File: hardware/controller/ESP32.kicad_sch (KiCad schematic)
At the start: 22 parts, among them J4 Conn_01x05_Pin, Q1 SS8050-G, Q2 SS8050-G, U2 ESP32-S3, Y1 FH4000074Z

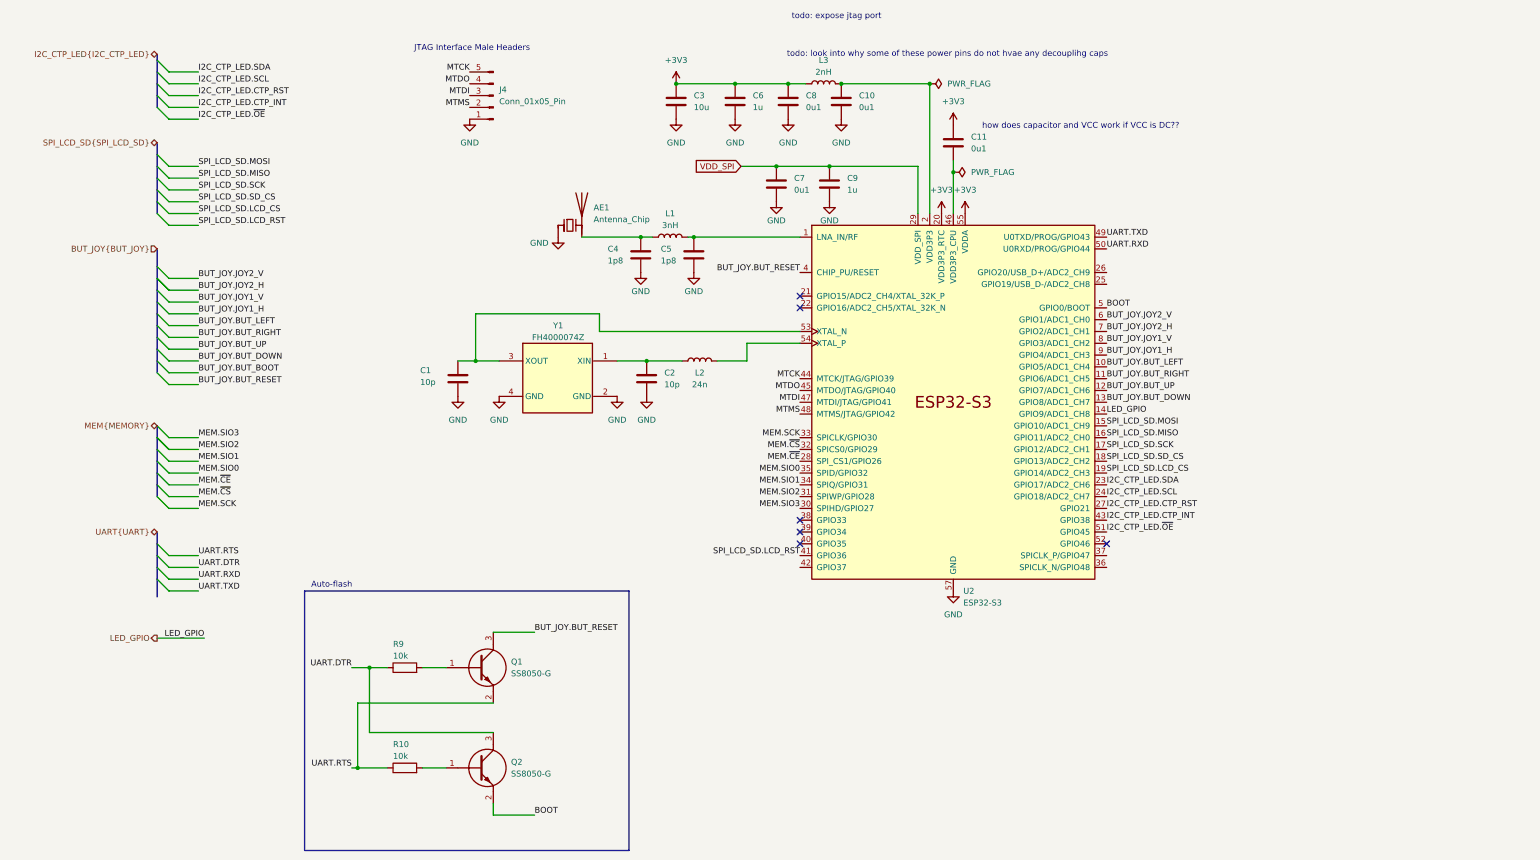
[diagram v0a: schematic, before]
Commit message: finished first rev of controller schematic minus actually finding passive components. moved some features to rev2 todo
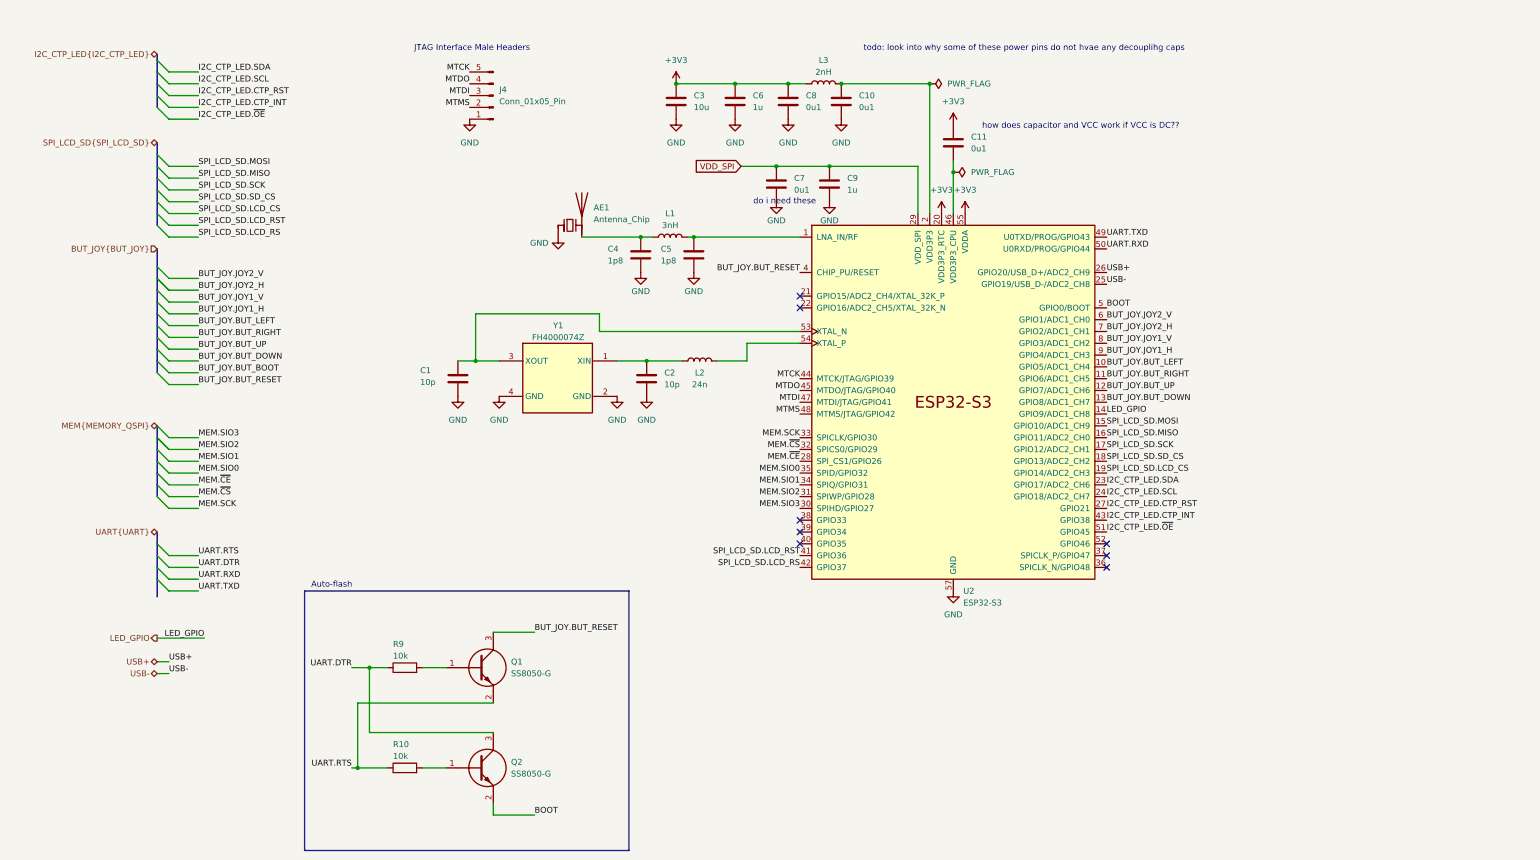
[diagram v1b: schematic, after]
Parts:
- AE1: footprint RF_Antenna:Texas_SWRA117D_2.4GHz_Right -> RF_Antenna:Texas_SWRA117D_2.4GHz_Left
- U2: footprint Package_DFN_QFN:QFN-56-1EP_7x7mm_P0.4mm_EP5.6x5.6mm -> SamacSys_Parts:QFN-56-1EP_7x7mm_P0.4mm_EP5.6x5.6mm
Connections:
- net USB-: now reaches U2.25 (GPIO19/USB_D-/ADC2_CH8)
- net USB+: now reaches U2.26 (GPIO20/USB_D+/ADC2_CH9)
- net SPI_LCD_SD.LCD_RS: now reaches U2.42 (GPIO37)
- no-connect marks 6 -> 8
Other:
- note added: "do i need these"
- note removed: "todo: expose jtag port"
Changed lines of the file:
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@@
 	(generator_version "9.0")
 	(paper "A4")
-	(bus_alias "MEMORY"
+	(bus_alias "MEMORY_QSPI"
 		(members "~{CS}" "~{CE}" "SIO0" "SCK" "SIO1" "SIO2" "SIO3")
 	)
@@
 	(text "todo: look into why some of these power pins do not hvae any decouplihg caps"
 		(exclude_from_sim no)
-		(at 213.36 22.86 0)
+		(at 229.87 21.59 0)
 		(effects
 			(font
@@
 		)
 	)
-	(text "todo: expose jtag port\n"
+	(text "do i need these"
 		(exclude_from_sim no)
-		(at 189.484 14.732 0)
+		(at 178.308 54.61 0)
 		(effects
 			(font
@@
 	)
 	(no_connect
+		(at 247.65 130.81)
+	)
+	(no_connect
 		(at 247.65 128.27)
 	)
@@
 	)
 	(no_connect
+		(at 247.65 133.35)
+	)
+	(no_connect
 		(at 181.61 123.19)
 	)
@@
 	)
 	(bus_entry
+		(at 43.18 59.69)
+		(size 2.54 2.54)
+		(stroke
+			(width 0)
+			(type default)
+		)
+	)
+	(bus_entry
 		(at 43.18 130.81)
 		(size 2.54 2.54)
@@
 	(wire
 		(pts
+			(xy 45.72 156.21) (xy 43.18 156.21)
+		)
+		(stroke
+			(width 0)
+			(type default)
+		)
+	)
+	(wire
+		(pts
 			(xy 45.72 107.95) (xy 52.07 107.95)
 		)
@@
 	(wire
 		(pts
+			(xy 45.72 62.23) (xy 52.07 62.23)
+		)
+		(stroke
+			(width 0)
+			(type default)
+		)
+	)
+	(wire
+		(pts
 			(xy 45.72 93.98) (xy 52.07 93.98)
 		)
@@
 		)
 	)
+	(wire
+		(pts
+			(xy 43.18 153.67) (xy 45.72 153.67)
+		)
+		(stroke
+			(width 0)
+			(type default)
+		)
+	)
 	(bus
 		(pts
@@
 		)
 	)
-	(wire
-		(pts
-			(xy 187.96 46.99) (xy 207.01 46.99)
-		)
-		(stroke
-			(width 0)
-			(type default)
-		)
-	)
 	(bus
 		(pts
@@
 	(wire
 		(pts
+			(xy 187.96 46.99) (xy 207.01 46.99)
+		)
+		(stroke
+			(width 0)
+			(type default)
+		)
+	)
+	(wire
+		(pts
 			(xy 138.43 82.55) (xy 138.43 78.74)
 		)
@@
 		)
 	)
+	(bus
+		(pts
+			(xy 43.18 57.15) (xy 43.18 59.69)
+		)
+		(stroke
+			(width 0)
+			(type default)
+		)
+	)
 	(label "MEM.SIO2"
 		(at 181.61 118.11 180)
@@
 		)
 	)
+	(label "USB-"
+		(at 45.72 156.21 0)
+		(effects
+			(font
+				(size 1.27 1.27)
+			)
+			(justify left bottom)
+		)
+	)
 	(label "BUT_JOY.JOY1_H"
 		(at 247.65 87.63 0)
@@
 		)
 	)
+	(label "USB+"
+		(at 247.65 69.85 0)
+		(effects
+			(font
+				(size 1.27 1.27)
+			)
+			(justify left bottom)
+		)
+	)
 	(label "BUT_JOY.BUT_LEFT"
 		(at 52.07 81.28 0)
@@
 		)
 	)
+	(label "SPI_LCD_SD.LCD_RS"
+		(at 181.61 133.35 180)
+		(effects
+			(font
+				(size 1.27 1.27)
+			)
+			(justify right bottom)
+		)
+	)
 	(label "BUT_JOY.JOY1_V"
 		(at 247.65 85.09 0)
@@
 		)
 	)
+	(label "USB+"
+		(at 45.72 153.67 0)
+		(effects
+			(font
+				(size 1.27 1.27)
+			)
+			(justify left bottom)
+		)
+	)
 	(label "I2C_CTP_LED.SDA"
 		(at 247.65 115.57 0)
@@
 		)
 	)
+	(label "SPI_LCD_SD.LCD_RS"
+		(at 52.07 62.23 0)
+		(effects
+			(font
+				(size 1.27 1.27)
+			)
+			(justify left bottom)
+		)
+	)
 	(label "MEM.SCK"
 		(at 181.61 105.41 180)
@@
 		)
 	)
+	(label "USB-"
+		(at 247.65 72.39 0)
+		(effects
+			(font
+				(size 1.27 1.27)
+			)
+			(justify left bottom)
+		)
+	)
 	(label "BUT_JOY.BUT_RIGHT"
 		(at 52.07 83.82 0)
@@
 		)
 	)
-	(hierarchical_label "MEM{MEMORY}"
+	(hierarchical_label "USB+"
+		(shape bidirectional)
+		(at 43.18 153.67 180)
+		(effects
+			(font
+				(size 1.27 1.27)
+			)
+			(justify right)
+		)
+	)
+	(hierarchical_label "MEM{MEMORY_QSPI}"
 		(shape bidirectional)
 		(at 43.18 102.87 180)
@@
 		)
 	)
+	(hierarchical_label "USB-"
+		(shape bidirectional)
+		(at 43.18 156.21 180)
+		(effects
+			(font
+				(size 1.27 1.27)
+			)
+			(justify right)
+		)
+	)
 	(hierarchical_label "SPI_LCD_SD{SPI_LCD_SD}"
 		(shape bidirectional)
@@
 			)
 		)
-		(property "Footprint" "RF_Antenna:Texas_SWRA117D_2.4GHz_Right"
+		(property "Footprint" "RF_Antenna:Texas_SWRA117D_2.4GHz_Left"
 			(at 129.54 55.245 0)
 			(effects
@@
 			)
 		)
-		(property "Footprint" "Package_DFN_QFN:QFN-56-1EP_7x7mm_P0.4mm_EP5.6x5.6mm"
+		(property "Footprint" "SamacSys_Parts:QFN-56-1EP_7x7mm_P0.4mm_EP5.6x5.6mm"
 			(at 214.63 146.05 0)
 			(effects

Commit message: Moved LEDs around. Replaced some discrete resistors with resistor arrays. Added mounting holes. Added. Added a lot of actual components for passive elements
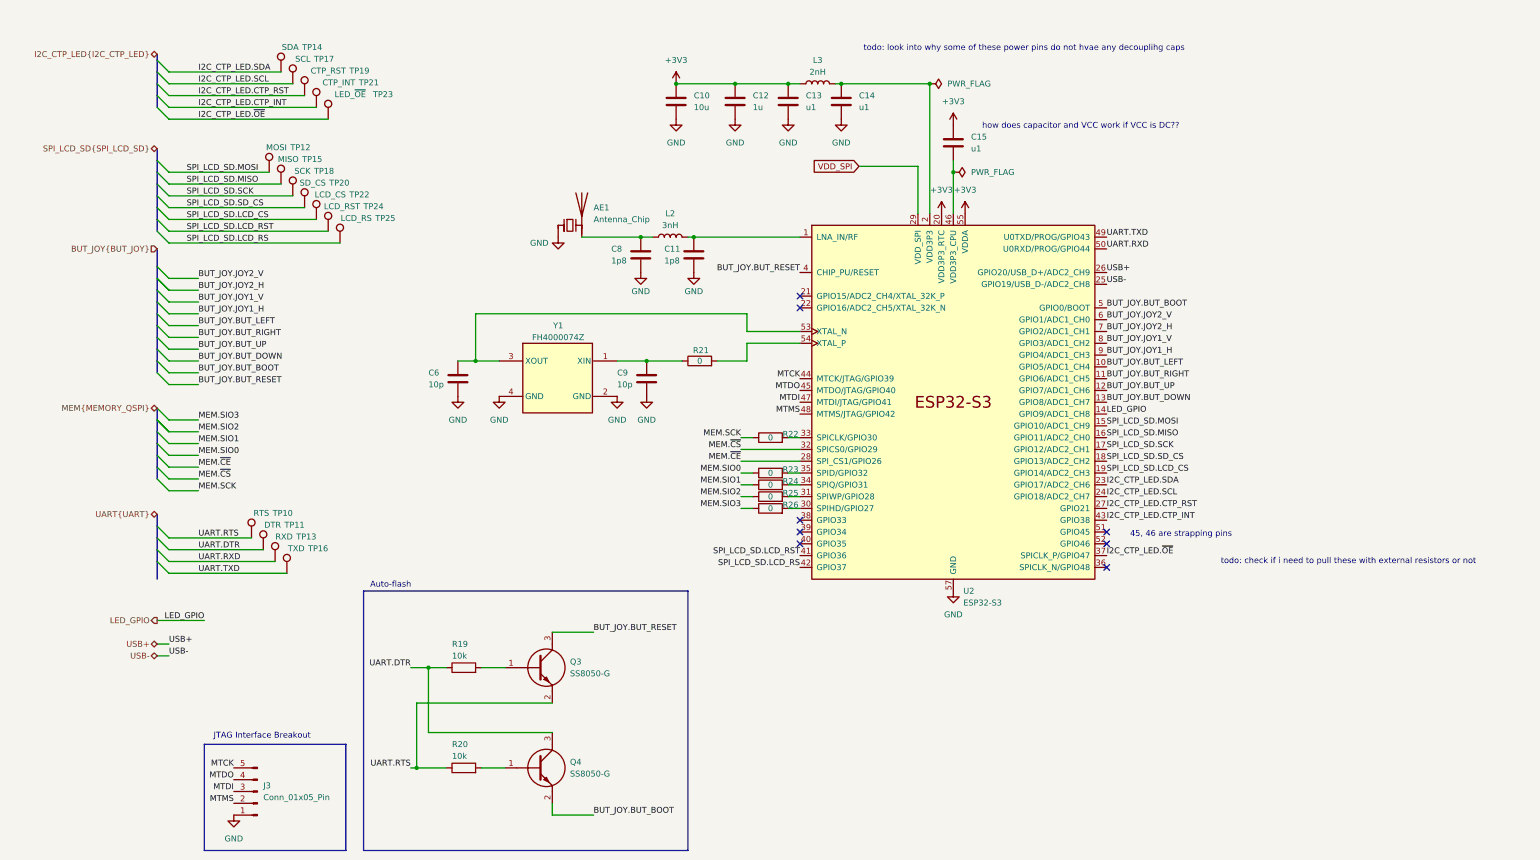
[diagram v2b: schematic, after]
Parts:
- removed C1, C2: 10p, symbol Device:C
- removed C4, C5: 1p8, symbol Device:C
- removed C7: 0u1, symbol Device:C
- removed L2: 24n, symbol Device:L
- added C11, C8: 1p8, Capacitor_SMD:C_0603_1608Metric, symbol Device:C
- added C6: 10p, GRT033, symbol Device:C
- added R21, R22, R23, R24, R25, R26: 0, RESC1608X50N, symbol Device:R
- added TP10: RTS, TestPoint:TestPoint_Pad_1.0x1.0mm, symbol Connector:TestPoint
- added TP11: DTR, TestPoint:TestPoint_Pad_1.0x1.0mm, symbol Connector:TestPoint
- added TP12: MOSI, TestPoint:TestPoint_Pad_1.0x1.0mm, symbol Connector:TestPoint
- added TP13: RXD, TestPoint:TestPoint_Pad_1.0x1.0mm, symbol Connector:TestPoint
- added TP14: SDA, TestPoint:TestPoint_Pad_1.0x1.0mm, symbol Connector:TestPoint
- added TP15: MISO, TestPoint:TestPoint_Pad_1.0x1.0mm, symbol Connector:TestPoint
- added TP16: TXD, TestPoint:TestPoint_Pad_1.0x1.0mm, symbol Connector:TestPoint
- added TP17: SCL, TestPoint:TestPoint_Pad_1.0x1.0mm, symbol Connector:TestPoint
- added TP18: SCK, TestPoint:TestPoint_Pad_1.0x1.0mm, symbol Connector:TestPoint
- added TP19: CTP_RST, TestPoint:TestPoint_Pad_1.0x1.0mm, symbol Connector:TestPoint
- added TP20: SD_CS, TestPoint:TestPoint_Pad_1.0x1.0mm, symbol Connector:TestPoint
- added TP21: CTP_INT, TestPoint:TestPoint_Pad_1.0x1.0mm, symbol Connector:TestPoint
- added TP22: LCD_CS, TestPoint:TestPoint_Pad_1.0x1.0mm, symbol Connector:TestPoint
- added TP23: LED_~{OE}, TestPoint:TestPoint_Pad_1.0x1.0mm, symbol Connector:TestPoint
- added TP24: LCD_RST, TestPoint:TestPoint_Pad_1.0x1.0mm, symbol Connector:TestPoint
- added TP25: LCD_RS, TestPoint:TestPoint_Pad_1.0x1.0mm, symbol Connector:TestPoint
- C10: renamed from C3; footprint (none) -> CAPC1608X80N; Height (none) -> 0.8; Manufacturer_Name (none) -> TDK; Manufacturer_Part_Number (none) -> C1608X7T1A106M080AC; Mouser Part Number (none) -> 810-C1608X7T1A106M08; Mouser Price/Stock (none) -> https://www.mouser.co.uk/ProductDetail/TDK/C1608X7T1A106M08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
- C12: renamed from C6; footprint (none) -> CAPC2012X135N; Height (none) -> 1.35; Manufacturer_Name (none) -> Walsin Technology Corporation; Manufacturer_Part_Number (none) -> 0805X105K160CT; Mouser Part Number (none) -> 791-0805X105K160CT; Mouser Price/Stock (none) -> https://www.mouser.co.uk/ProductDetail/Walsin/0805X105K160C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
- C13: renamed from C8; value 0u1 -> u1; footprint (none) -> MAJx16; Height (none) -> 0.8; Manufacturer_Name (none) -> TAIYO YUDEN; Manufacturer_Part_Number (none) -> MAJCH168BB7104KTEA01; Mouser Part Number (none) -> 963-MAJCH168BB7104KT; Mouser Price/Stock (none) -> https://www.mouser.co.uk/ProductDetail/TAIYO-YUDEN/MAJCH168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
- C14: renamed from C10; value 0u1 -> u1; footprint (none) -> MAJx16; Height (none) -> 0.8; Manufacturer_Name (none) -> TAIYO YUDEN; Manufacturer_Part_Number (none) -> MAJCH168BB7104KTEA01; Mouser Part Number (none) -> 963-MAJCH168BB7104KT; Mouser Price/Stock (none) -> https://www.mouser.co.uk/ProductDetail/TAIYO-YUDEN/MAJCH168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
- C15: renamed from C11; value 0u1 -> u1; footprint (none) -> MAJx16; Height (none) -> 0.8; Manufacturer_Name (none) -> TAIYO YUDEN; Manufacturer_Part_Number (none) -> MAJCH168BB7104KTEA01; Mouser Part Number (none) -> 963-MAJCH168BB7104KT; Mouser Price/Stock (none) -> https://www.mouser.co.uk/ProductDetail/TAIYO-YUDEN/MAJCH168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
- C9: value 1u -> 10p; footprint (none) -> GRT033; Height (none) -> 0.33; Manufacturer_Name (none) -> Murata Electronics; Manufacturer_Part_Number (none) -> GRT0335C1H100GA02D
- Q3: renamed from Q1; footprint SamacSys_Parts:SOT95P240X115-3N -> SOT95P240X115-3N
- Q4: renamed from Q2; footprint SamacSys_Parts:SOT95P240X115-3N -> SOT95P240X115-3N
- R19: renamed from R9; footprint (none) -> RESC2012X60N; Height (none) -> 0.6; Manufacturer_Name (none) -> TT Electronics; Manufacturer_Part_Number (none) -> ASC0805-10KFT5; Mouser Part Number (none) -> 756-ASC0805-10KFT5; Mouser Price/Stock (none) -> https://www.mouser.co.uk/ProductDetail/Welwyn-Components-TT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
- R20: renamed from R10; footprint (none) -> RESC2012X60N; Height (none) -> 0.6; Manufacturer_Name (none) -> TT Electronics; Manufacturer_Part_Number (none) -> ASC0805-10KFT5; Mouser Part Number (none) -> 756-ASC0805-10KFT5; Mouser Price/Stock (none) -> https://www.mouser.co.uk/ProductDetail/Welwyn-Components-TT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
- U2: footprint SamacSys_Parts:QFN-56-1EP_7x7mm_P0.4mm_EP5.6x5.6mm -> Package_DFN_QFN:QFN-56-1EP_7x7mm_P0.4mm_EP5.6x5.6mm
- Y1: footprint SamacSys_Parts:FH4000074Z -> FH4000074Z
- renumbered J4 to J3, L1 to L2
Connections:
- net BOOT is gone; now on net BUT_JOY.BUT_BOOT: Q4.2 (E), U2.5 (GPIO0/BOOT)
- net GND: now also C11.2, C6.2, C8.2
- net I2C_CTP_LED.CTP_INT: now also TP21.1
- net I2C_CTP_LED.CTP_RST: now also TP19.1
- net I2C_CTP_LED.SCL: now also TP17.1
- net I2C_CTP_LED.SDA: now also TP14.1
- net I2C_CTP_LED.~{OE}: now also U2.37 (SPICLK_P/GPIO47), TP23.1; no longer U2.51 (GPIO45)
- net MEM.SCK: now also R22.1; no longer U2.33 (SPICLK/GPIO30)
- net MEM.SIO0: now also R23.1; no longer U2.35 (SPID/GPIO32)
- net MEM.SIO1: now also R24.1; no longer U2.34 (SPIQ/GPIO31)
- net MEM.SIO2: now also R25.1; no longer U2.31 (SPIWP/GPIO28)
- net MEM.SIO3: now also R26.1; no longer U2.30 (SPIHD/GPIO27)
- net SPI_LCD_SD.LCD_CS: now also TP22.1
- net SPI_LCD_SD.LCD_RS: now also TP25.1
- net SPI_LCD_SD.LCD_RST: now also TP24.1
- net SPI_LCD_SD.MISO: now also TP15.1
- net SPI_LCD_SD.MOSI: now also TP12.1
- net SPI_LCD_SD.SCK: now also TP18.1
- net SPI_LCD_SD.SD_CS: now also TP20.1
- net UART.DTR: now also TP11.1
- net UART.RTS: now also TP10.1
- net UART.RXD: now also TP13.1
- net UART.TXD: now also TP16.1
- net VDD_SPI: no longer C9.1
- net at U2.53 (XTAL_N), Y1.3 (XOUT): now also C6.1
- net at AE1.2 (PCB_Trace), L2.1: now also C8.1
- net at L2.2, U2.1 (LNA_IN/RF): now also C11.1
- net at Y1.1 (XIN): now also C9.1, R21.1
- net at U2.54 (XTAL_P): now also R21.2
- new net: R23.2, U2.35 (SPID/GPIO32)
- new net: R26.2, U2.30 (SPIHD/GPIO27)
- new net: R24.2, U2.34 (SPIQ/GPIO31)
- new net: R25.2, U2.31 (SPIWP/GPIO28)
- new net: R22.2, U2.33 (SPICLK/GPIO30)
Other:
- note added: "45, 46 are strapping pins"
- note added: "JTAG Interface Breakout"
- note added: "todo: check if i need to pull these with external resistors or not"
- note removed: "JTAG Interface Male Headers"
- note removed: "do i need these"
- moved on the sheet: J3, L3, Q3, Q4, R19, R20
